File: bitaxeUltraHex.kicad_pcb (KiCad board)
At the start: 4 copper layers, 84.5 x 129.5 mm, 334 parts, among them J1 Conn_01x01, J2 Conn_01x01, J3 TC2030-IDC, J4 USB_C_Receptacle_USB2.0, J5 Conn_01x04, J6 Conn_01x04, J7 Conn_01x04, Q1 NTMFS5C673NLT1G, Q2 CSD17577Q5A, Q3 NTMFS5C673NLT1G, Q4 CSD17577Q5A, Q5 BSS123, SW1 GT-TC029B-H025-L1N, SW2 GT-TC029B-H025-L1N, U1 uA7805, U10 TMP1075, U11 TMP1075, U12 EMC2302, U13 BM1366_mode1, U14 ADP171AUJ-R7, U15 ADP171AUJ-R7, U16 BM1366_mode1, U17 25MHz, U18 TLV3544, U19 BM1366_mode0, U2 RT9080-33GJ5, U20 ADP171AUJ-R7, U21 ADP171AUJ-R7, U22 BM1366_mode0, U23 TLV3544, U24 BM1366_mode1, U25 ADP171AUJ-R7, U26 ADP171AUJ-R7, U27 BM1366_mode1, U3 INA219AIDCNR, U4 TPS40305, U5 MIC5504, U6 DS4432U+, U7 SN74AVC4T774, U8 176x320_st7789, U9 ESP32-S3-WROOM-1, Y1 32.768kHz

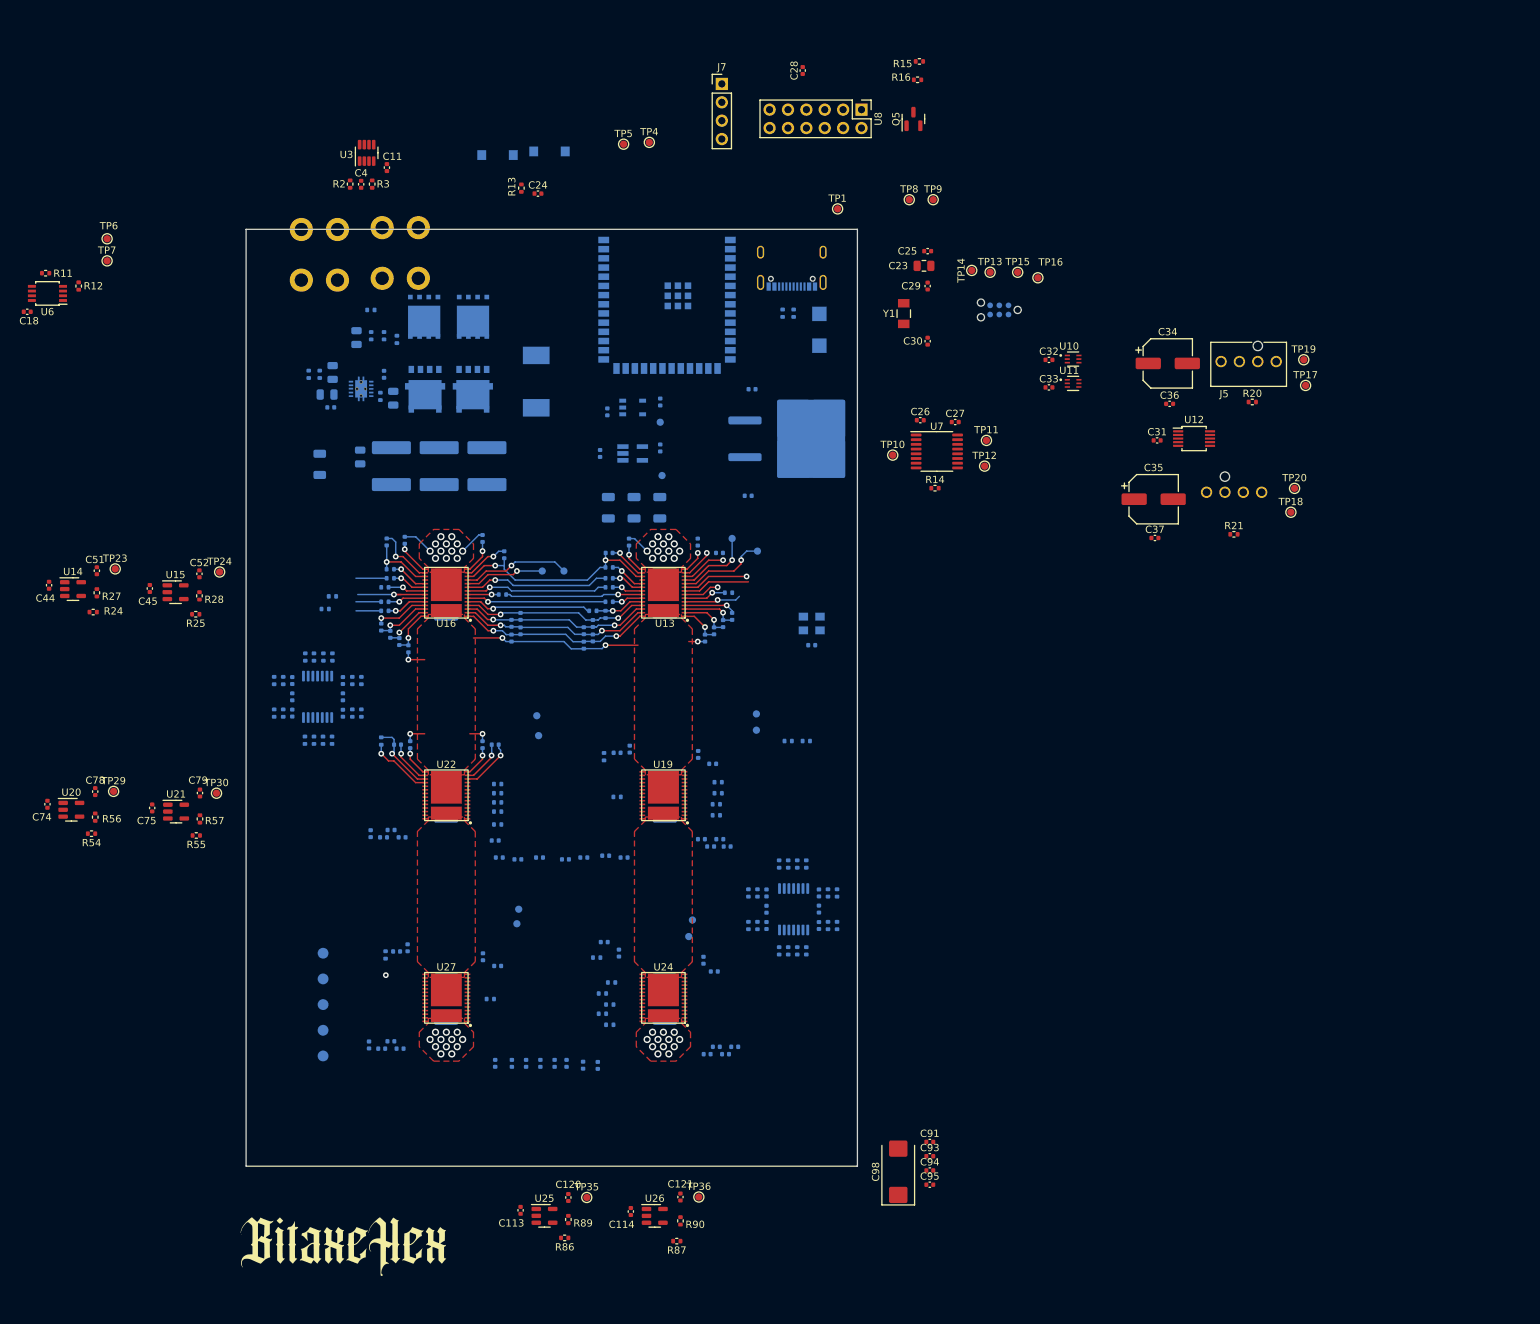
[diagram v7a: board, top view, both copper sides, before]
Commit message: major rework of the power supply section
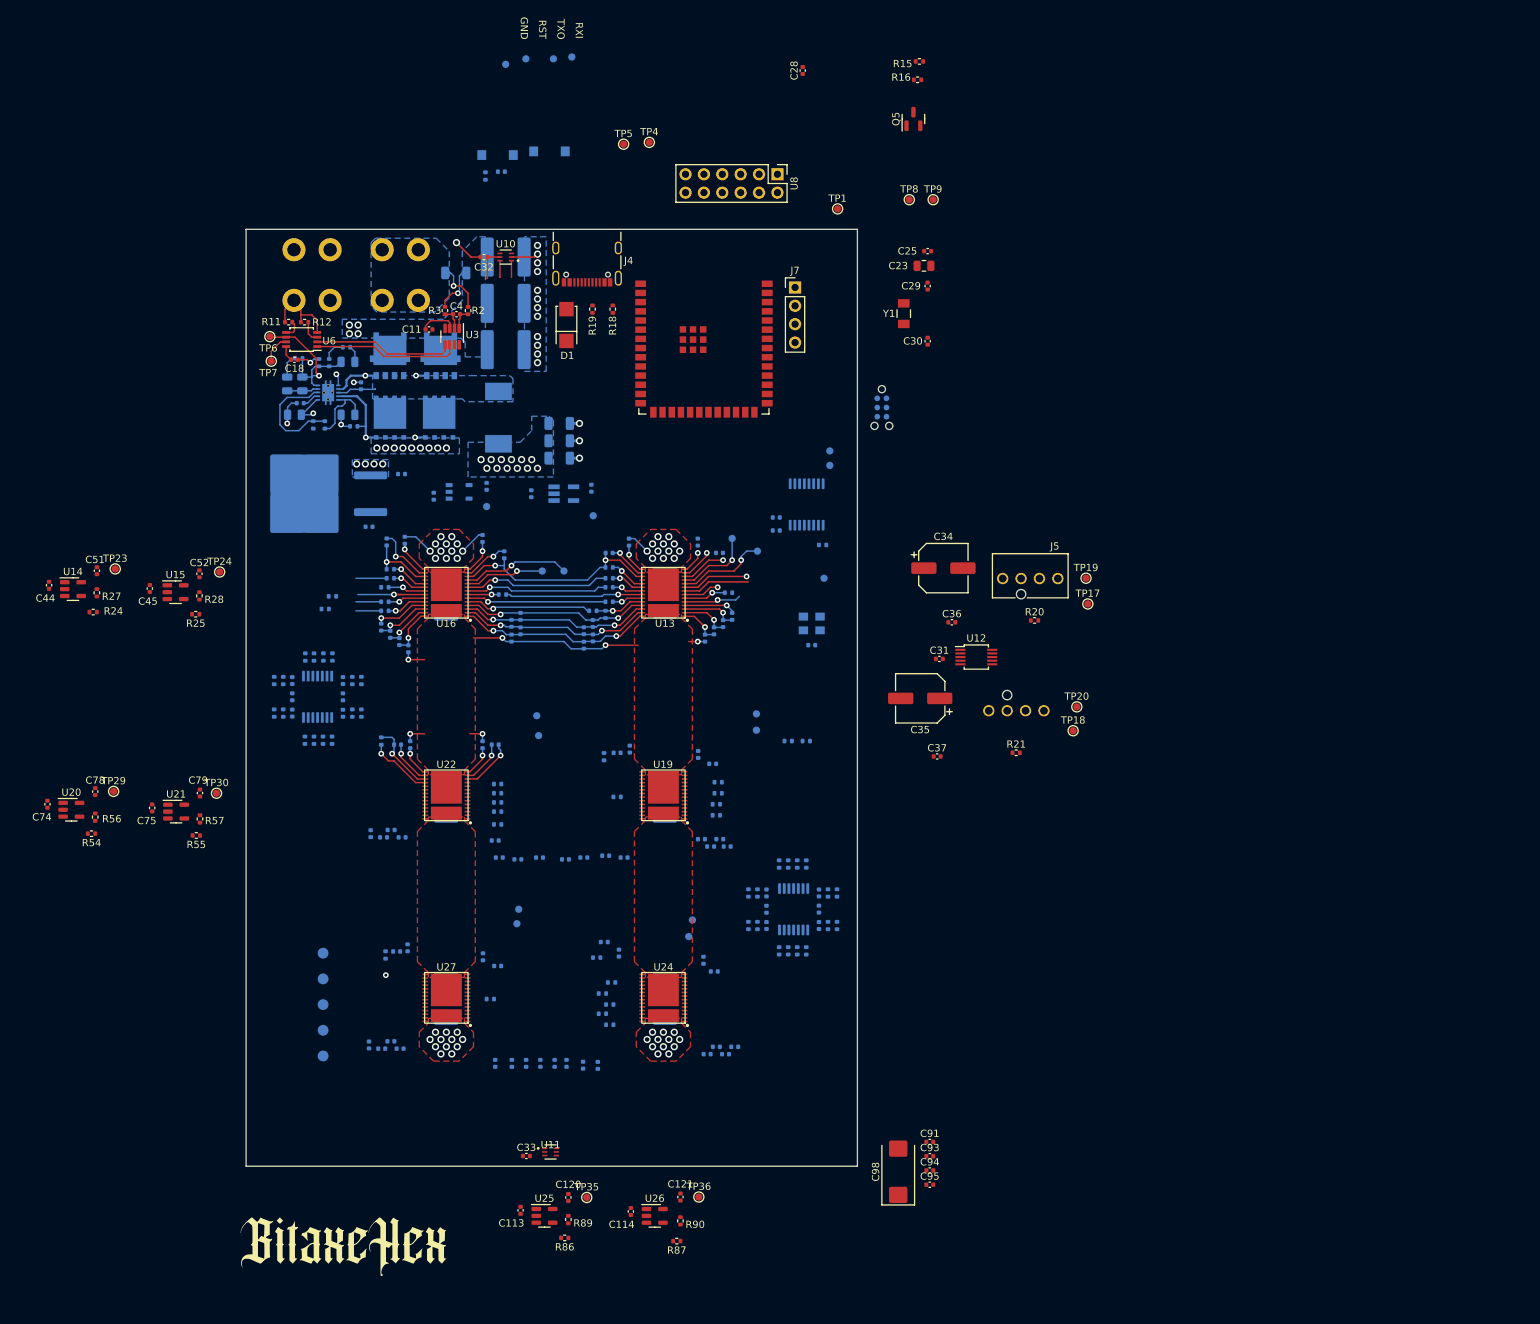
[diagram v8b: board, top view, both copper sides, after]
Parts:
- C24, C26, C27, R13, R14, TP10, TP11, TP12, TP13, TP14, TP15, TP16, U7: moved to B.Cu
- D1, J4, R18, R19, U9: moved to F.Cu
- moved U11 128.5 mm to (92.4, 174.3)
- moved C33 128.5 mm to (89.1, 174.9)
- moved U10 79.7 mm to (86.2, 50.6), turned to 180 degrees
- moved C32 79.4 mm to (83.2, 50.6), turned to 180 degrees
- moved TP16 79.3 mm to (86.2, 24.0), turned to 180 degrees
- moved TP15 74.1 mm to (89.0, 23.2), turned to 180 degrees
- moved U1 67.5 mm to (59.9, 83.3), turned to 180 degrees
- moved TP13 67.2 mm to (92.8, 23.2), turned to 180 degrees
- moved TP14 62.7 mm to (95.3, 22.9)
- moved C12 56.3 mm to (67.3, 87.9)
- moved C3 48.0 mm to (71.8, 80.6), turned to 180 degrees
- moved TP19 42.6 mm to (166.4, 95.0)
- moved C31 42.6 mm to (146.1, 106.1)
- moved C36 42.6 mm to (147.9, 101.1)
- moved C37 42.6 mm to (145.8, 119.6)
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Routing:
- net GND: track 11.2 -> 49.2 mm, vias 24 -> 52
- net /SDA: track 0.00 -> 22.6 mm
- net /Power/OUT0: track 0.00 -> 22.4 mm, vias 0 -> 1
- net /SCL: track 0.00 -> 21.7 mm
- net Net-(Q2-G): track 0.00 -> 19.8 mm, vias 0 -> 2
- net /Power/VIN_M: track 0.00 -> 16.6 mm, vias 0 -> 10
- net /Power/PGOOD: track 0.00 -> 15.8 mm
- net Net-(Q1-G): track 0.00 -> 15.0 mm, vias 0 -> 2
- net Net-(U4-BP): track 0.00 -> 9.92 mm
- net /Power/VIN: track 0.00 -> 7.19 mm, vias 0 -> 1
- net /3V3: track 0.00 -> 6.86 mm
- net Net-(U4-BOOT): track 0.00 -> 5.82 mm, vias 0 -> 2
- net /Power/SW: track 0.00 -> 5.37 mm
- net Net-(U4-COMP): track 0.00 -> 4.36 mm
- net /Power/OUT1: track 0.00 -> 3.98 mm
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- added copper zone on B.Cu, net /Power/SW
- added copper zone on B.Cu, net /Power/VIN
- added copper zone on B.Cu, net /Power/VIN_M
- added copper zone on In1.Cu, net /Power/VIN_M
- added copper zone on B.Cu, net /VDD
- added copper zone on B.Cu, net GND
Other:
- board text added: "+V"
